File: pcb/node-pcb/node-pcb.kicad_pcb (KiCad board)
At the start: 2 copper layers, 52 x 51 mm, 34 parts, among them J1 10103594-0001LF, J2 TSW-102-07-G-S, J3 TSW-118-07-L-D, J4 TSW-118-07-L-D, U1 NCP1117ST33T3G, U2 W25Q128JVSIQ, U3 RP2040, X1 12MHz

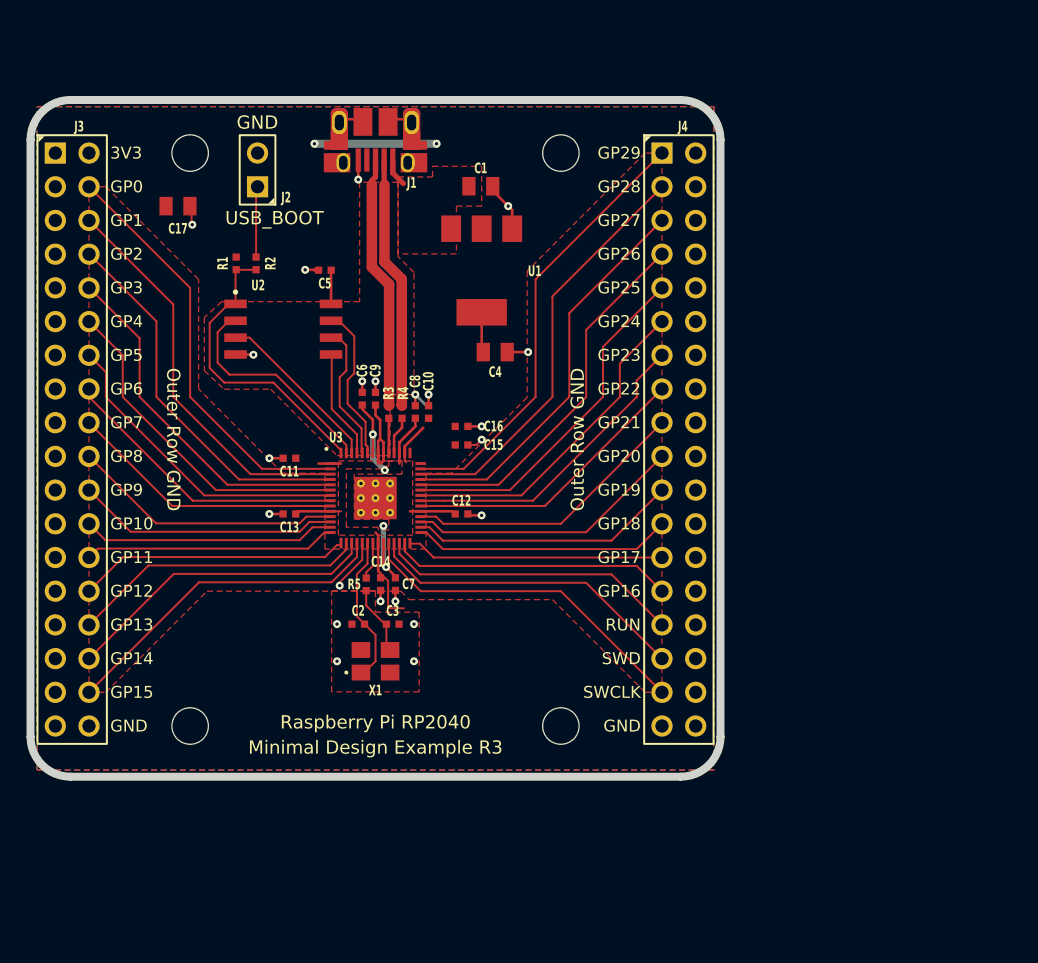
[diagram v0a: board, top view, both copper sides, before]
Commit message: Add BOM CSV and schematic PDF for node-pcb design
- Created a new BOM CSV file detailing components used in the node-pcb project, including specifications such as reference, description, quantity, part numbers, and links to datasheets.
- Added a new schematic PDF file for the node-pcb design to provide a visual representation of the circuit layout.
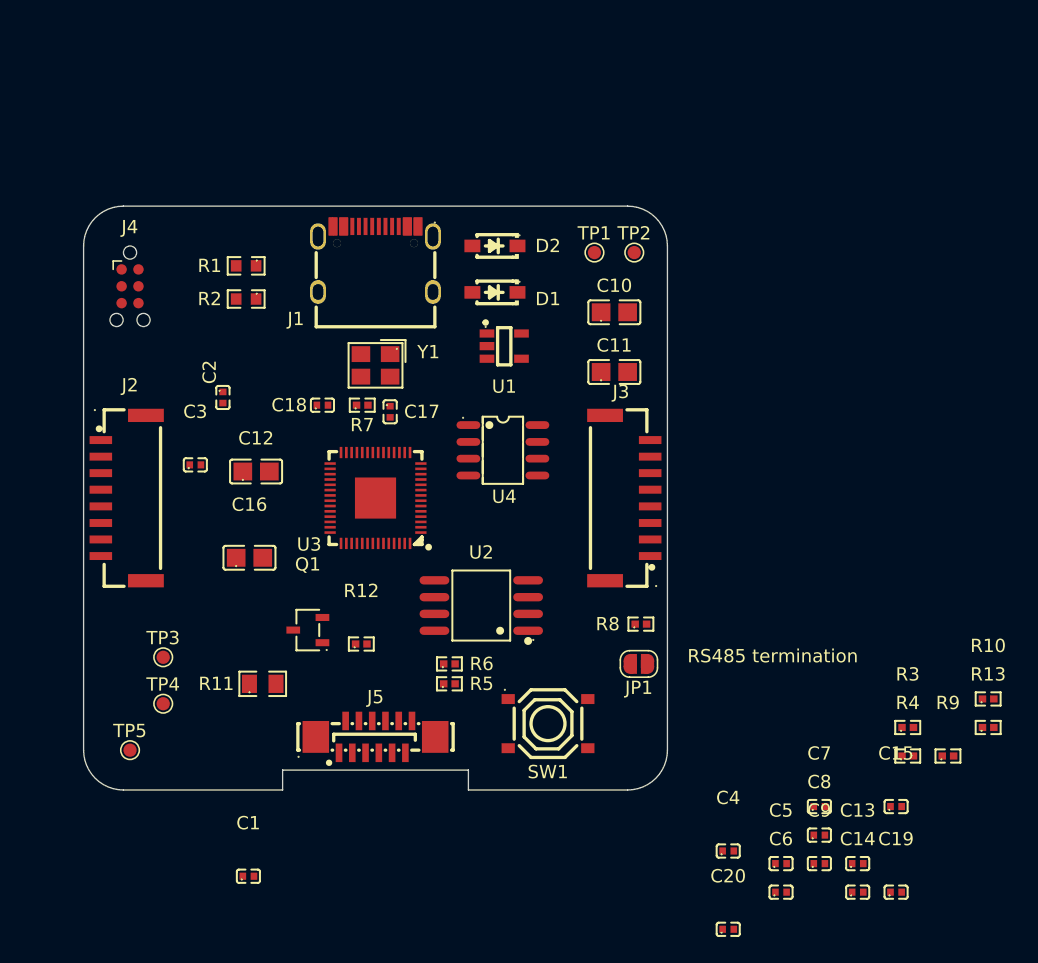
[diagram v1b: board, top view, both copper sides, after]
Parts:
- removed MH1, MH2, MH3, MH4: NPTH FD2.75mm SM3.15mm KO6mm, RPI_COMPILED:none_mh_npth_fd2p75mm_sm3p15mm_ko6mm
- added C18: 15pF, JLCPCB:C0402, F.Cu at (96.0, 93.0)
- added C19: 1uF, JLCPCB:C0402, F.Cu at (139.2, 129.7)
- added C20: 100nF, JLCPCB:C0402, F.Cu at (126.6, 132.5)
- added D1: B5819WSL, JLCPCB:SOD-123_L2.7-W1.6-LS3.7-RD-1, F.Cu at (109.0, 84.5)
- added D2: B5819WSL, JLCPCB:SOD-123_L2.7-W1.6-LS3.7-RD-1, F.Cu at (109.0, 81.0)
- added J5: AFC11-S12ICA-00, JLCPCB:CONN-SMD-12P_AFC11-S12ICA-00, F.Cu at (100.0, 118.0)
- added JP1: Solder Jumper, Jumper:SolderJumper-2_P1.3mm_Open_RoundedPad1.0x1.5mm, F.Cu at (119.8, 112.5)
- added Q1: S8050, JLCPCB:SOT-23-3_L3.0-W1.7-P0.95-LS2.9-BR, F.Cu at (94.9, 110.0)
- added R10: 10k, JLCPCB:R0402, F.Cu at (146.2, 115.1)
- added R11: 47, JLCPCB:R0805, F.Cu at (91.5, 114.0)
- added R12: 2.2k, JLCPCB:R0402, F.Cu at (98.9, 111.0)
- added R13: 10k, JLCPCB:R0402, F.Cu at (146.2, 117.3)
- added R6: 1k, JLCPCB:R0402, F.Cu at (105.6, 112.5)
- added R7: 1k, JLCPCB:R0402, F.Cu at (99.0, 93.0)
- added R8: 120, JLCPCB:R0402, F.Cu at (120.0, 109.5)
- added R9: 10k, JLCPCB:R0402, F.Cu at (143.1, 119.4)
- added SW1: TS-1187A-B-A-B, JLCPCB:SW-SMD_4P-L5.1-W5.1-P3.70-LS6.5-TL_H1.5, F.Cu at (113.0, 117.0)
- added TP1: TP_5V, TestPoint:TestPoint_Pad_D1.0mm, F.Cu at (116.5, 81.5)
- added TP2: TP_3V3, TestPoint:TestPoint_Pad_D1.0mm, F.Cu at (119.5, 81.5)
- added TP3: TP_1V1, TestPoint:TestPoint_Pad_D1.0mm, F.Cu at (84.0, 112.0)
- added TP4: TP_A, TestPoint:TestPoint_Pad_D1.0mm, F.Cu at (84.0, 115.5)
- added TP5: TP_B, TestPoint:TestPoint_Pad_D1.0mm, F.Cu at (81.5, 119.0)
- added U4: THVD1450DR, JLCPCB:SOIC-8_L4.9-W3.9-P1.27-LS6.0-BL, F.Cu at (109.6, 96.4)
- C1, C4: value 10u -> 100nF; footprint RPI_COMPILED:generic_capc2012x125 -> JLCPCB:C0402
- C10: value 1u -> 10uF; footprint RPI_COMPILED:generic_capc1005x50 -> JLCPCB:C0805
- C11, C12, C16: value 100n -> 10uF; footprint RPI_COMPILED:generic_capc1005x50 -> JLCPCB:C0805
- C13, C14: value 100n -> 1uF; footprint RPI_COMPILED:generic_capc1005x50 -> JLCPCB:C0402
- C15, C5, C6, C7, C9: value 100n -> 100nF; footprint RPI_COMPILED:generic_capc1005x50 -> JLCPCB:C0402
- C17: value 10u -> 15pF; footprint RPI_COMPILED:generic_capc2012x125 -> JLCPCB:C0402
- C2, C3: value 15p -> 100nF; footprint RPI_COMPILED:generic_capc1005x50 -> JLCPCB:C0402
- C8: value 1u -> 100nF; footprint RPI_COMPILED:generic_capc1005x50 -> JLCPCB:C0402
- J1: value 10103594-0001LF -> TYPE-C-31-M-12; footprint RPI_COMPILED:amphenol_10103594-0001lf -> JLCPCB:USB-C_SMD-TYPE-C-31-M-12_1
- J2: value TSW-102-07-G-S -> BM08B-GHS-TBT(LF)(SN); footprint RPI_COMPILED:samtec_tsw-102-07-g-s -> JLCPCB:CONN-SMD_BM08B-GHS-TBT-LF-SN
- J3: value TSW-118-07-L-D -> BM08B-GHS-TBT(LF)(SN); footprint RPI_COMPILED:samtec_tsw-118-07-l-d -> JLCPCB:CONN-SMD_BM08B-GHS-TBT-LF-SN
- J4: value TSW-118-07-L-D -> TC2030; footprint RPI_COMPILED:samtec_tsw-118-07-l-d -> Connector:Tag-Connect_TC2030-IDC-NL_2x03_P1.27mm_Vertical
- R1: value 1k -> 5.1k; footprint RPI_COMPILED:generic_resc1005x35 -> JLCPCB:R0603
- R2: value 10k -> 5.1k; footprint RPI_COMPILED:generic_resc1005x35 -> JLCPCB:R0603
- R3, R4: value 27 -> 33; footprint RPI_COMPILED:generic_resc1005x35 -> JLCPCB:R0402
- R5: value 1k -> 10k; footprint RPI_COMPILED:generic_resc1005x35 -> JLCPCB:R0402
- U1: value NCP1117ST33T3G -> AP2112K-3.3; footprint RPI_COMPILED:onsemi_ncp1117st33t3g -> JLCPCB:SOT-25-5_L2.9-W1.6-P0.95-LS2.8-BL
- U2: value W25Q128JVSIQ -> W25Q32JVSSIQ; footprint RPI_COMPILED:generic_soic127p790x195-8 -> JLCPCB:SOIC-8_L5.3-W5.3-P1.27-LS8.0-BL
- U3: footprint RPI_COMPILED:rpi_rp2040_vias -> JLCPCB:LQFN-56_L7.0-W7.0-P0.4-EP
- Y1: renamed from X1; value 12MHz -> ABM8-272-T3; footprint RPI_COMPILED:generic_xtalcc320x250x80-4 -> JLCPCB:CRYSTAL-SMD_4P-L3.2-W2.5-BL
- moved C5 56.4 mm to (130.6, 127.5), turned to 0 degrees
- moved C1 54.9 mm to (90.4, 128.5)
- moved C13 50.3 mm to (136.3, 127.5), turned to 0 degrees
- moved C6 48.8 mm to (130.6, 129.7), turned to 0 degrees
- moved C9 48.4 mm to (133.4, 127.5), turned to 0 degrees
- moved R4 46.1 mm to (140.1, 119.4), turned to 0 degrees
- moved R3 45.8 mm to (140.1, 117.3), turned to 0 degrees
- moved C8 44.1 mm to (133.4, 125.4), turned to 0 degrees
- moved J4 42.9 mm to (81.5, 84.0)
- moved C14 42.8 mm to (136.3, 129.7), turned to 0 degrees
- moved C15 42.6 mm to (139.2, 123.2)
- moved J3 42.1 mm to (119.0, 100.0)
- moved C4 41.5 mm to (126.6, 126.6)
- moved C7 36.1 mm to (133.4, 123.2), turned to 0 degrees
- moved J2 26.7 mm to (81.0, 100.0)
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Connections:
- C1 pad 1: VBUS -> +1V1
- C11 pad 1: +3V3 -> /5V_LOCAL
- C14 pad 1: +3V3 -> +1V1
- C16 pad 1: +3V3 -> GND
- C16 pad 2: GND -> VBUS +5V
- C17 pad 1: +3V3 -> GND
- C17 pad 2: GND -> /XIN
- C2 pad 1: /XIN -> +1V1
- C3 pad 1: Net-(C3-Pad1) -> +3V3
- C6 pad 1: +1V1 -> +3V3
- C7 pad 1: +1V1 -> +3V3
- C8 pad 1: +1V1 -> +3V3
- J1 pad 1: VBUS -> (no net)
- J1 pad 2: /USB_D- -> (no net)
- J1 pad 3: /USB_D+ -> (no net)
- J1 pad 4: unconnected-(J1-ID-Pad4) -> (no net)
- J2 pad 1: /~{USB_BOOT} -> GND
- J2 pad 2: GND -> VBUS +5V
- J3 pad 10: /GPIO3 -> GND
- J3 pad 2: +3V3 -> VBUS +5V
- J3 pad 3: GND -> VBUS +5V
- J3 pad 4: /GPIO0 -> GND
- J3 pad 5: GND -> /RS485_A
- J3 pad 6: /GPIO1 -> /RS485_B
- J3 pad 7: GND -> /ADDR_IN
- J3 pad 8: /GPIO2 -> /SPARE_IN
- J4 pad 1: /GPIO29_ADC3 -> +3V3
- J4 pad 2: GND -> /SWDIO
- J4 pad 3: /GPIO28_ADC2 -> /RUN
- J4 pad 4: GND -> /SWCLK
- J4 pad 5: /GPIO27_ADC1 -> GND
- R1 pad 1: /QSPI_SS -> /USB-C_CC1
- R1 pad 2: /~{USB_BOOT} -> GND
- R2 pad 1: +3V3 -> /USB-C_CC2
- R2 pad 2: /QSPI_SS -> GND
- R3 pad 1: /USB_D+ -> /USB_MCU_D+
- R3 pad 2: Net-(U3-USB_DP) -> /USB_D+
- R4 pad 1: /USB_D- -> /USB_MCU_D-
- R4 pad 2: Net-(U3-USB_DM) -> /USB_D-
- R5 pad 1: Net-(C3-Pad1) -> +3V3
- R5 pad 2: /XOUT -> /QSPI_SS
- U1 pad 1: GND -> /5V_LOCAL
- U1 pad 2: +3V3 -> GND
- U1 pad 3: VBUS -> /5V_LOCAL
- U1 pad 4: +3V3 -> unconnected-(U1-NC-Pad4)
- U3 pad 11: /GPIO8 -> /SPARE_OUT
- U3 pad 12: /GPIO9 -> /SPARE_IN
- U3 pad 13: /GPIO10 -> /ADDR_OUT
- U3 pad 14: /GPIO11 -> /ADDR_IN
- U3 pad 15: /GPIO12 -> /GPIO12_TX
- U3 pad 16: /GPIO13 -> /GPIO13_RX
- U3 pad 17: /GPIO14 -> /GPIO14_RE
- U3 pad 18: /GPIO15 -> /GPIO15_DE
- U3 pad 2: /GPIO0 -> unconnected-(U3-GPIO0-Pad2)
- U3 pad 25: /SWD -> /SWDIO
- U3 pad 27: /GPIO16 -> /RESET
- U3 pad 28: /GPIO17 -> /D/C
- U3 pad 29: /GPIO18 -> /SPI0_SCK (SCL)
- U3 pad 3: /GPIO1 -> unconnected-(U3-GPIO1-Pad3)
- U3 pad 30: /GPIO19 -> /SPI0_TX (MOSI)
- U3 pad 31: /GPIO20 -> /CS
- U3 pad 32: /GPIO21 -> /BL_PWM
- U3 pad 34: /GPIO22 -> unconnected-(U3-GPIO22-Pad34)
- U3 pad 35: /GPIO23 -> unconnected-(U3-GPIO23-Pad35)
- U3 pad 36: /GPIO24 -> unconnected-(U3-GPIO24-Pad36)
- U3 pad 37: /GPIO25 -> unconnected-(U3-GPIO25-Pad37)
- U3 pad 38: /GPIO26_ADC0 -> unconnected-(U3-GPIO26_ADC0-Pad38)
- U3 pad 39: /GPIO27_ADC1 -> unconnected-(U3-GPIO27_ADC1-Pad39)
- U3 pad 4: /GPIO2 -> unconnected-(U3-GPIO2-Pad4)
- U3 pad 40: /GPIO28_ADC2 -> unconnected-(U3-GPIO28_ADC2-Pad40)
- U3 pad 41: /GPIO29_ADC3 -> unconnected-(U3-GPIO29_ADC3-Pad41)
- U3 pad 46: Net-(U3-USB_DM) -> /USB_MCU_D-
- U3 pad 47: Net-(U3-USB_DP) -> /USB_MCU_D+
- U3 pad 5: /GPIO3 -> unconnected-(U3-GPIO3-Pad5)
- U3 pad 6: /GPIO4 -> unconnected-(U3-GPIO4-Pad6)
- U3 pad 7: /GPIO5 -> unconnected-(U3-GPIO5-Pad7)
- U3 pad 8: /GPIO6 -> unconnected-(U3-GPIO6-Pad8)
- U3 pad 9: /GPIO7 -> unconnected-(U3-GPIO7-Pad9)
- Y1 pad 3: Net-(C3-Pad1) -> Net-(C18-Pad2)
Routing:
- net +3V3: track 41.0 -> 0.00 mm, vias 2 -> 0
- net /GPIO29_ADC3: track 33.2 -> 0.00 mm
- net /GPIO0: track 31.8 -> 0.00 mm
- net /GPIO28_ADC2: track 31.6 -> 0.00 mm
- net /GPIO1: track 30.2 -> 0.00 mm
- net /GPIO27_ADC1: track 29.9 -> 0.00 mm
- net GND: track 29.7 -> 0.00 mm, vias 22 -> 0
- net /GPIO2: track 28.5 -> 0.00 mm
- net /GPIO26_ADC0: track 28.3 -> 0.00 mm
- net /GPIO3: track 26.9 -> 0.00 mm
- net /GPIO25: track 26.7 -> 0.00 mm
- net /SWCLK: track 25.9 -> 0.00 mm
- net /GPIO15: track 25.4 -> 0.00 mm
- net /GPIO4: track 25.3 -> 0.00 mm
- net /GPIO24: track 25.0 -> 0.00 mm
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- removed copper zone on F.Cu, net +1V1
- removed copper zone on F.Cu, net +3V3
- removed copper zone on B.Cu, net GND
- removed copper zone on F.Cu, net GND
- removed copper zone on F.Cu, net VBUS
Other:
- board size 52 x 51 mm -> 44 x 44 mm
- copper layers 2 -> 4
- board text added: "RS485 termination"
- board text removed: "3V3"
- board text removed: "GND"
- board text removed: "GP0"
- board text removed: "GP1"
- board text removed: "GP10"
- board text removed: "GP11"
- board text removed: "GP12"
- board text removed: "GP13"
- board text removed: "GP14"
- board text removed: "GP15"
- board text removed: "GP16"
- board text removed: "GP17"
- board text removed: "GP18"
- board text removed: "GP19"
- board text removed: "GP2"
- board text removed: "GP20"
- board text removed: "GP21"
- board text removed: "GP22"
- board text removed: "GP23"
- board text removed: "GP24"
- board text removed: "GP25"
- board text removed: "GP26"
- board text removed: "GP27"
- board text removed: "GP28"
- board text removed: "GP29"
- board text removed: "GP3"
- board text removed: "GP4"
- board text removed: "GP5"
- board text removed: "GP6"
- board text removed: "GP7"
- board text removed: "GP8"
- board text removed: "GP9"
- board text removed: "Minimal Design Example R3"
- board text removed: "Outer Row GND"
- board text removed: "RUN"
- board text removed: "Raspberry Pi RP2040"
- board text removed: "SWCLK"
- board text removed: "SWD"
- board text removed: "USB_BOOT"

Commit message: Update schematic PDF with latest design revisions
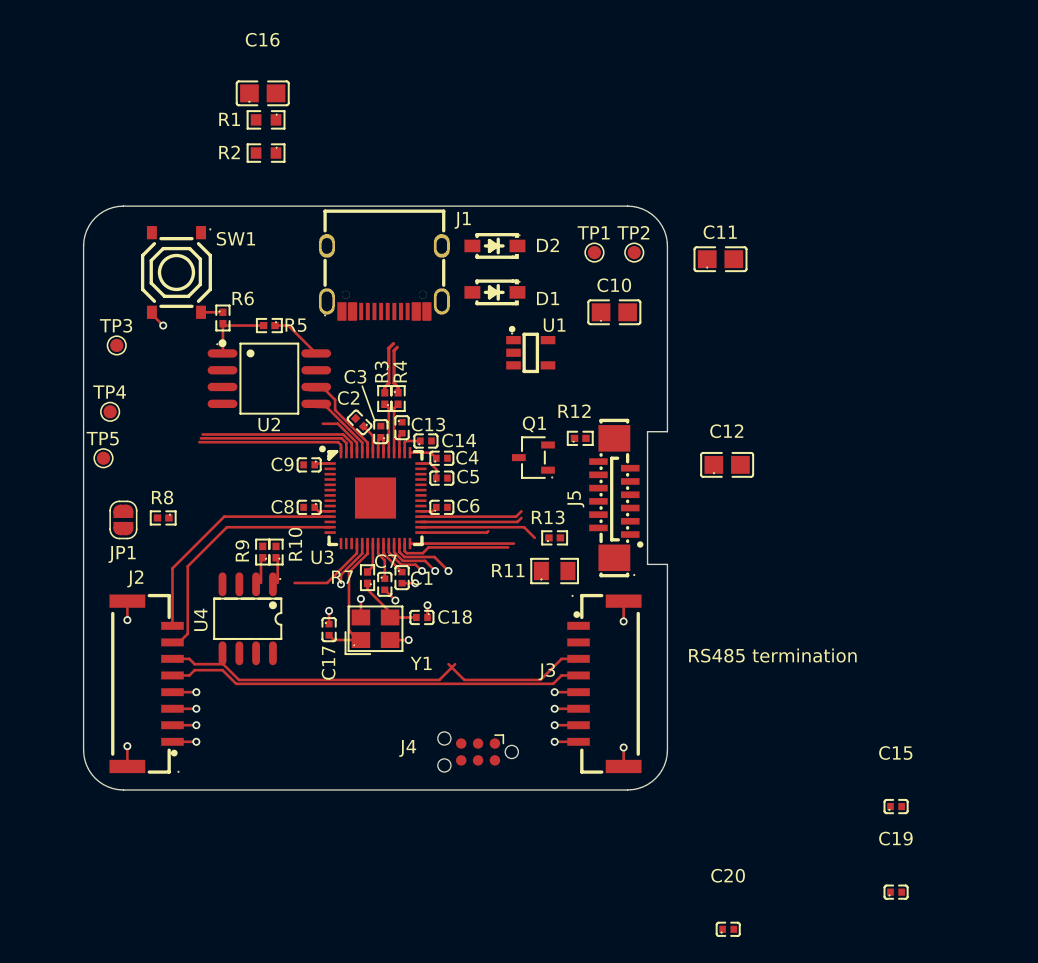
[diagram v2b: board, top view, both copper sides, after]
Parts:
- moved R10 54.8 mm to (92.5, 104.1), turned to 90 degrees
- moved R9 53.9 mm to (91.5, 104.1), turned to 90 degrees
- moved C9 48.8 mm to (95.0, 97.5), turned to 180 degrees
- moved C13 47.5 mm to (102.0, 94.7), turned to -90 degrees
- moved C14 47.1 mm to (103.8, 95.7)
- moved R4 46.9 mm to (101.7, 92.5), turned to -90 degrees
- moved R3 46.6 mm to (100.7, 92.5), turned to 90 degrees
- moved C8 45.7 mm to (95.0, 100.7), turned to 180 degrees
- moved SW1 44.0 mm to (85.0, 83.0), turned to -90 degrees
- moved J4 43.8 mm to (107.7, 119.1), turned to 180 degrees
- moved JP1 40.3 mm to (81.0, 101.7), turned to -90 degrees
- moved C5 38.7 mm to (105.0, 98.5)
- moved C6 38.7 mm to (105.0, 100.7)
- moved R8 36.9 mm to (84.0, 101.5), turned to 180 degrees
- moved C7 36.8 mm to (100.7, 106.5), turned to -90 degrees
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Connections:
- C13 pad 1: +3V3 -> GND
- C13 pad 2: GND -> +1V1
- C14 pad 1: +1V1 -> +3V3
- J2 pad 5: /RS485_A -> /RS485_P
- J2 pad 6: /RS485_B -> /RS485_N
- J3 pad 1: GND -> /SPARE_IN
- J3 pad 2: VBUS +5V -> /ADDR_IN
- J3 pad 3: VBUS +5V -> /RS485_N
- J3 pad 4: GND -> /RS485_P
- J3 pad 5: /RS485_A -> GND
- J3 pad 6: /RS485_B -> VBUS +5V
- J3 pad 7: /ADDR_IN -> VBUS +5V
- J3 pad 8: /SPARE_IN -> GND
- JP1 pad 2: /RS485_B -> /RS485_N
- R4 pad 1: /USB_MCU_D- -> /USB_D-
- R4 pad 2: /USB_D- -> /USB_MCU_D-
- R8 pad 1: /RS485_A -> /RS485_P
- R9 pad 1: /GPIO15_DE -> /GPIO13_DE
- TP4 pad 1: /RS485_A -> /RS485_P
- TP5 pad 1: /RS485_B -> /RS485_N
- U3 pad 12: /SPARE_IN -> unconnected-(U3-GPIO9-Pad12)
- U3 pad 16: /GPIO13_RX -> /GPIO13_DE
- U3 pad 18: /GPIO15_DE -> /GPIO15_RX
- U3 pad 37: unconnected-(U3-GPIO25-Pad37) -> /SPARE_IN
- U4 pad 1: /GPIO13_RX -> /GPIO15_RX
- U4 pad 3: /GPIO15_DE -> /GPIO13_DE
- U4 pad 6: /RS485_A -> /RS485_P
- U4 pad 7: /RS485_B -> /RS485_N
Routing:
- net /RS485_N: track 0.00 -> 33.4 mm
- net /RS485_P: track 0.00 -> 31.5 mm
- net GND: track 0.00 -> 25.4 mm, vias 0 -> 16
- net +3V3: track 0.00 -> 19.2 mm
- net /ADDR_OUT: track 0.00 -> 18.5 mm
- net /SPARE_OUT: track 0.00 -> 17.8 mm
- net /QSPI_SS: track 0.00 -> 16.7 mm
- net /QSPI_SD2: track 0.00 -> 12.2 mm
- net /QSPI_SD1: track 0.00 -> 11.8 mm
- net /XIN: track 0.00 -> 11.7 mm
- net /SPI0_TX (MOSI): track 0.00 -> 8.91 mm
- net /RESET: track 0.00 -> 8.61 mm
- net /D/C: track 0.00 -> 7.83 mm
- net /BL_PWM: track 0.00 -> 7.75 mm
- net /CS: track 0.00 -> 7.70 mm
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- added copper zone on In1.Cu, net GND
- added copper zone on In2.Cu, net VBUS +5V
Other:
- outline, holes or cut-outs redrawn
- board text added: "C52923"

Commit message: Refactor PCB and schematic files for improved clarity and functionality
- Updated PCB netclass assignments from "Power" to "Default" for better consistency.
- Changed PCB color settings to transparent for the "Power" netclass.
- Adjusted clearance value for the "QSPI" netclass from 0.3 to 0.2.
- Removed redundant no_connect entries and added a new no_connect entry in the schematic.
- Added new wire connections in the schematic for better signal integrity.
- Renamed label "ADDR_IN" to "SPARE_IN" and adjusted its position, while creating a new "ADDR_IN" label at a different location.
- Cleaned up used designators in the PCB file for better organization.
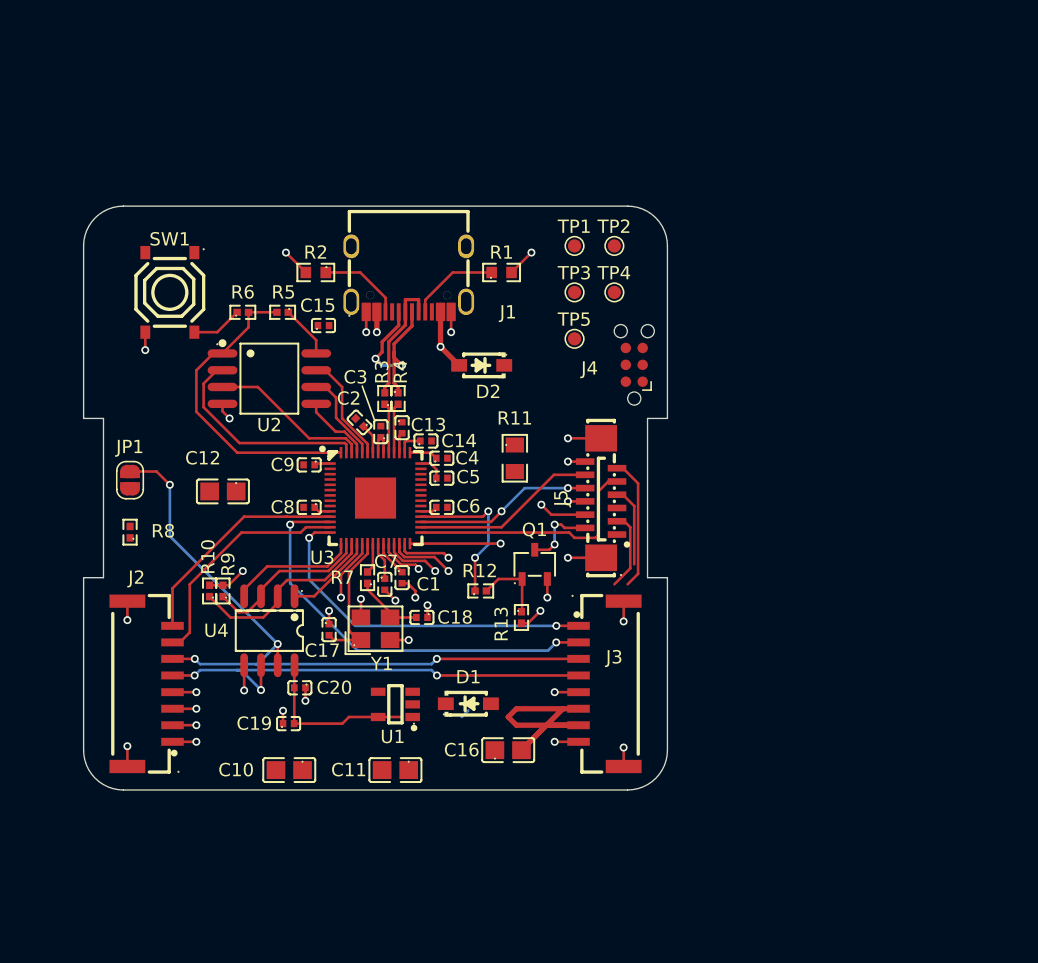
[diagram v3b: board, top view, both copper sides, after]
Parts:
- moved C15 56.4 mm to (96.1, 87.0)
- moved C16 52.8 mm to (110.0, 119.0)
- moved C19 47.5 mm to (93.5, 117.0)
- moved C11 45.6 mm to (101.5, 120.5), turned to 180 degrees
- moved C10 42.3 mm to (93.5, 120.5), turned to 180 degrees
- moved TP4 39.1 mm to (118.0, 84.5)
- moved C12 38.1 mm to (88.5, 99.5), turned to 180 degrees
- moved C20 37.1 mm to (94.3, 114.3), turned to 180 degrees
- moved TP5 36.6 mm to (115.0, 88.0)
- moved TP3 34.7 mm to (115.0, 84.5)
- moved J4 31.5 mm to (119.5, 90.0), turned to 90 degrees
- moved D1 31.1 mm to (107.0, 115.5), turned to 0 degrees
- moved U1 28.4 mm to (101.5, 115.5), turned to 90 degrees
- moved R1 21.1 mm to (109.5, 83.0), turned to 0 degrees
- moved R12 13.7 mm to (107.9, 107.0)
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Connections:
- U3 pad 12: unconnected-(U3-GPIO9-Pad12) -> /ADDR_IN
- U3 pad 14: /ADDR_IN -> /SPARE_IN
- U3 pad 37: /SPARE_IN -> unconnected-(U3-GPIO25-Pad37)
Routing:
- net /ADDR_IN: track 0.00 -> 31.6 mm, vias 0 -> 2
- net GND: track 25.4 -> 53.8 mm, vias 16 -> 31
- net /SPARE_IN: track 0.00 -> 26.6 mm, vias 0 -> 2
- net /RS485_N: track 33.4 -> 53.7 mm, vias 0 -> 4
- net VBUS +5V: track 7.20 -> 24.2 mm, vias 4 -> 2
- net +3V3: track 19.2 -> 35.5 mm, vias 0 -> 1
- net /SPI0_SCK (SCL): track 5.12 -> 18.6 mm
- net /GPIO14_RE: track 1.95 -> 14.7 mm
- net /VBUS_USB-C: track 0.00 -> 11.4 mm, vias 0 -> 2
- net /USB_D-: track 3.65 -> 14.5 mm, vias 0 -> 2
- net /GPIO13_DE: track 1.95 -> 12.8 mm
- net /GPIO12_TX: track 0.00 -> 9.66 mm
- net /QSPI_SS: track 16.7 -> 23.9 mm
- net /USB-C_CC1: track 0.00 -> 6.76 mm
- net /USB-C_CC2: track 0.00 -> 6.36 mm
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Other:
- outline, holes or cut-outs redrawn
- board text removed: "C52923"
- board text removed: "RS485 termination"
